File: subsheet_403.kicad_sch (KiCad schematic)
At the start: 44 parts, among them Q404 2N3904, Q405 2N3904, U403 MC1377_COLOR_TELEVISION_RGB_T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

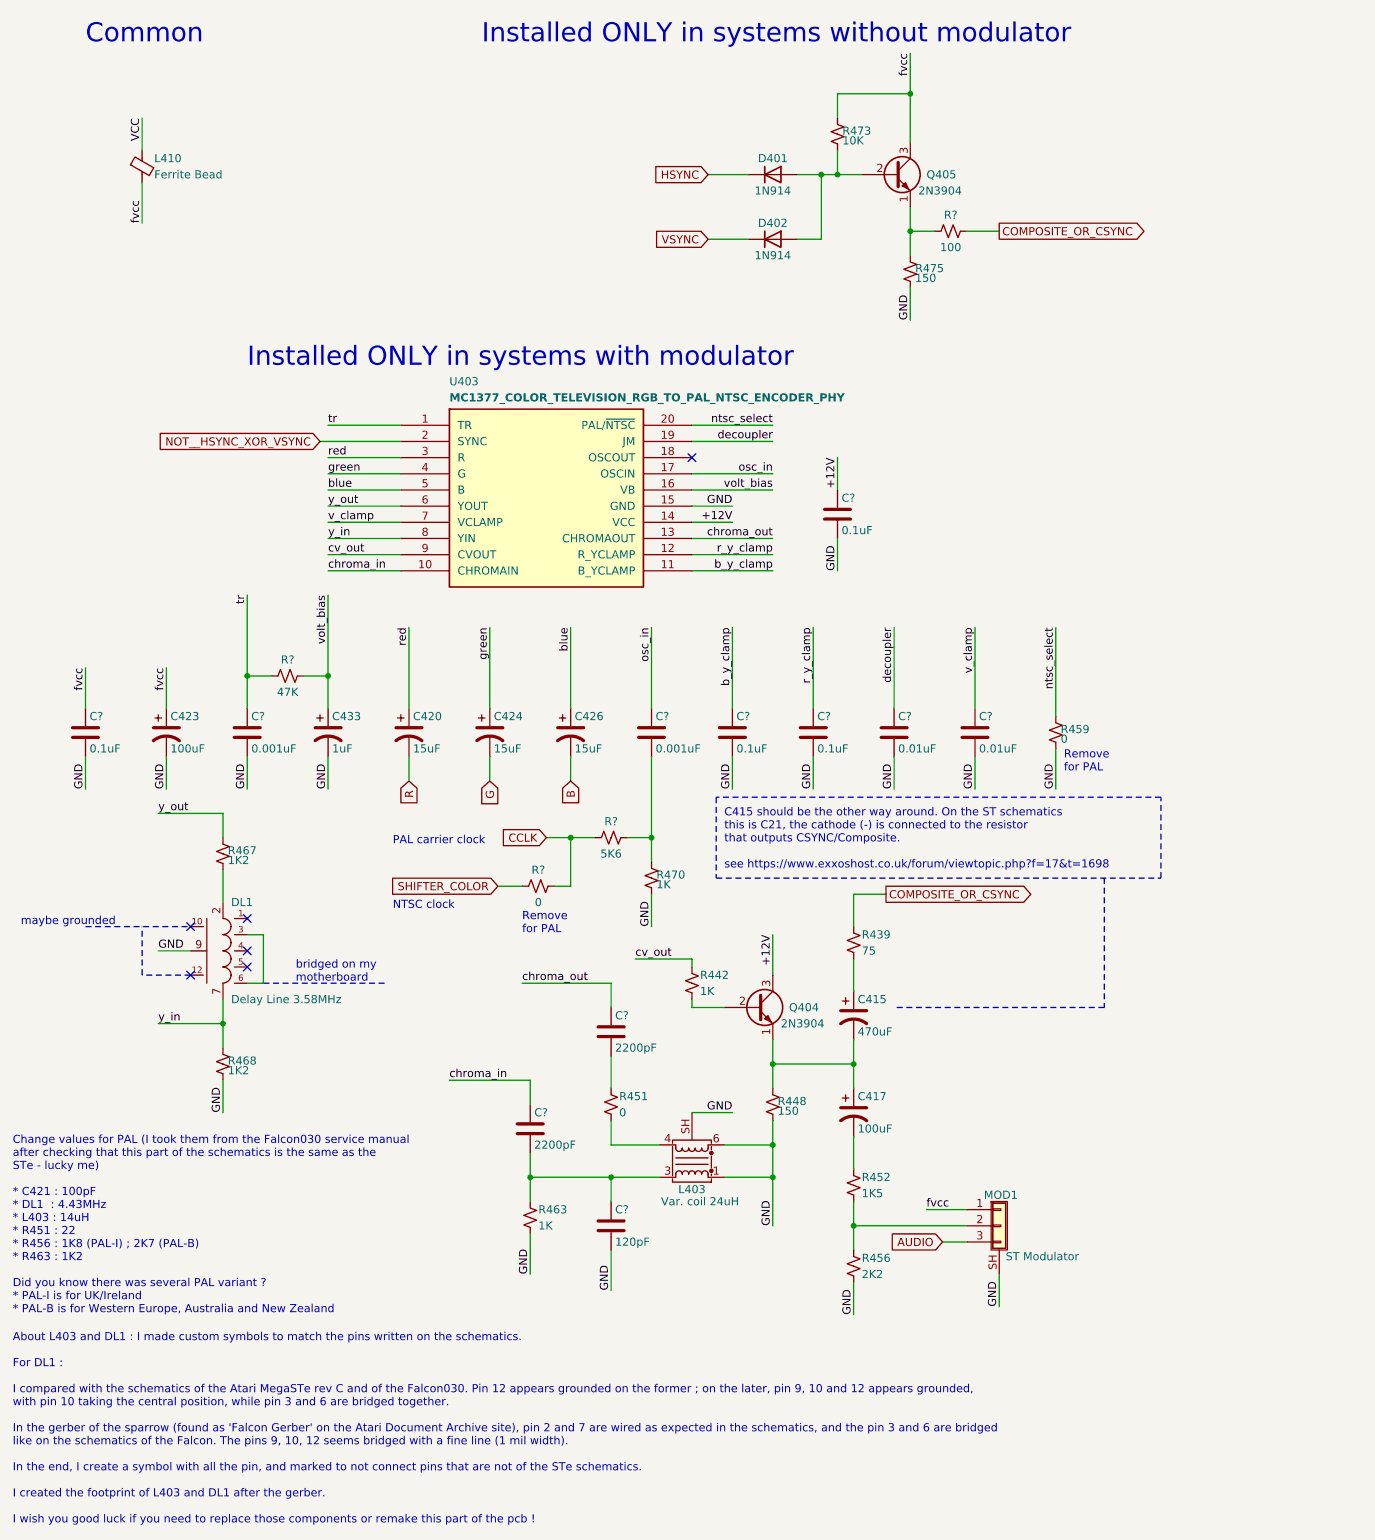
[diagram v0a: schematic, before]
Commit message: Resolves #3 : [schematic] annotate video port with signal name
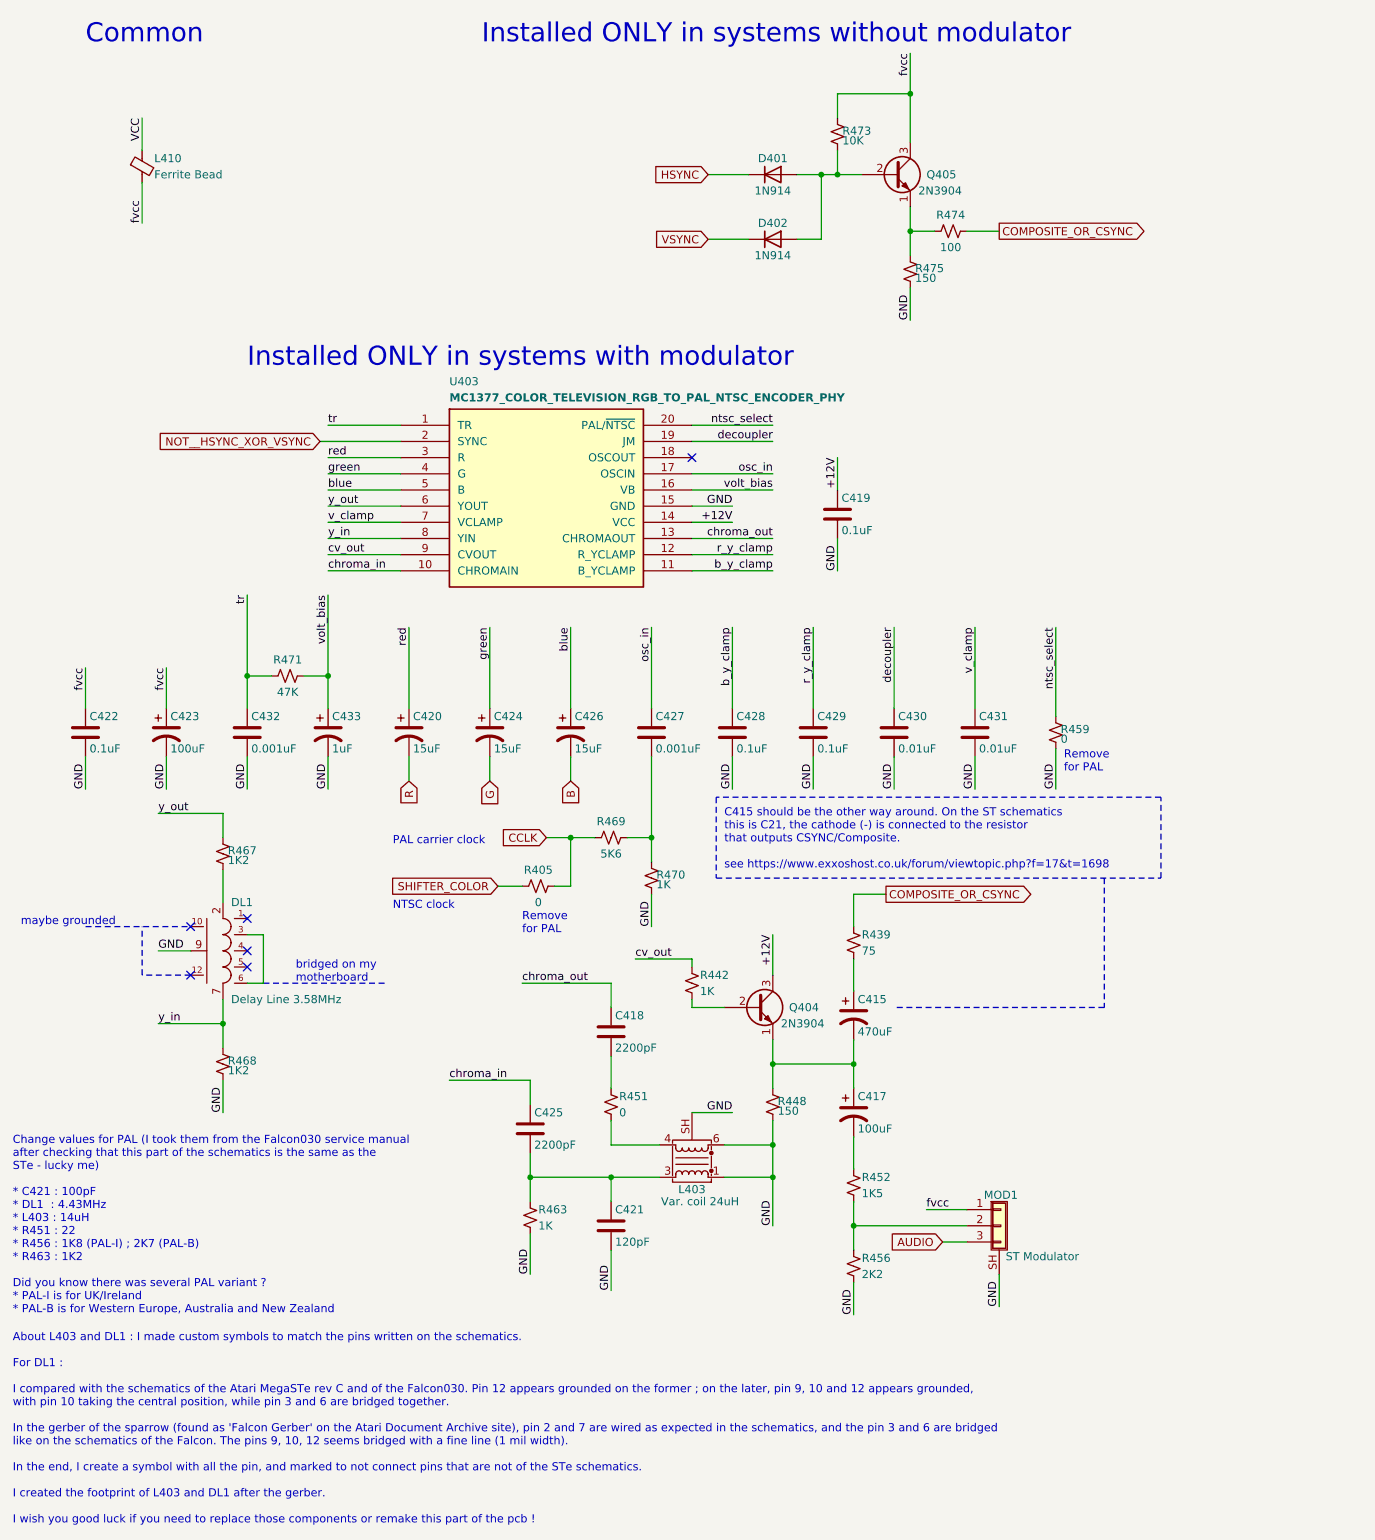
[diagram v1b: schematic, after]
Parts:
- gave numbers to parts that had none: 15
